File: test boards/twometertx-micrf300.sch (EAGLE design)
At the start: 12 parts

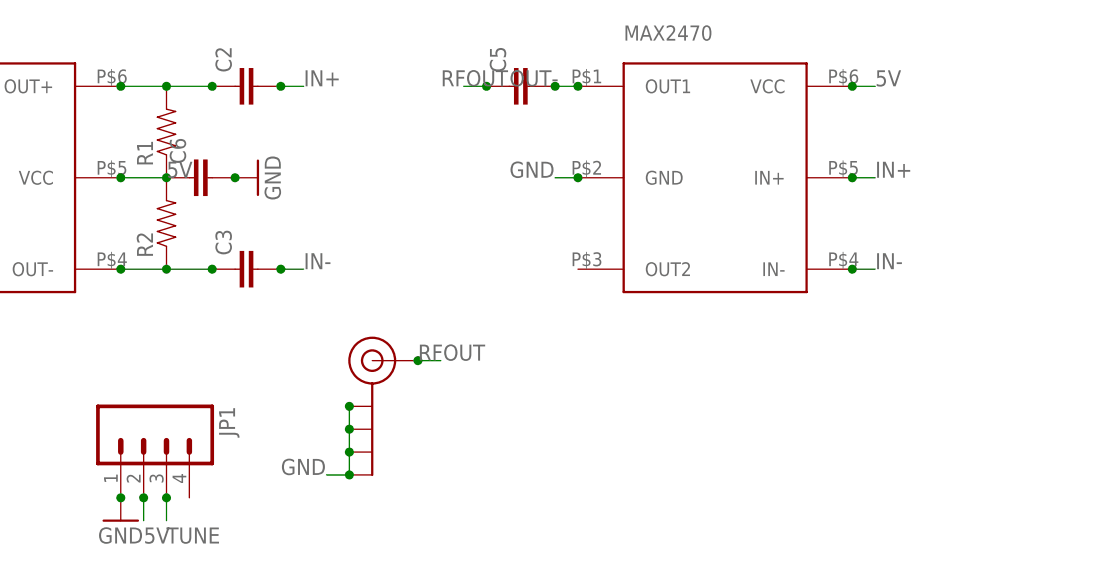
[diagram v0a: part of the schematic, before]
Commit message: updates
added twometertx-micrf300, changed layout of twometertx, changed led
layout on programmer shield to correct an error, added tracksoar v1.1
to swap power and ground pins on power input header
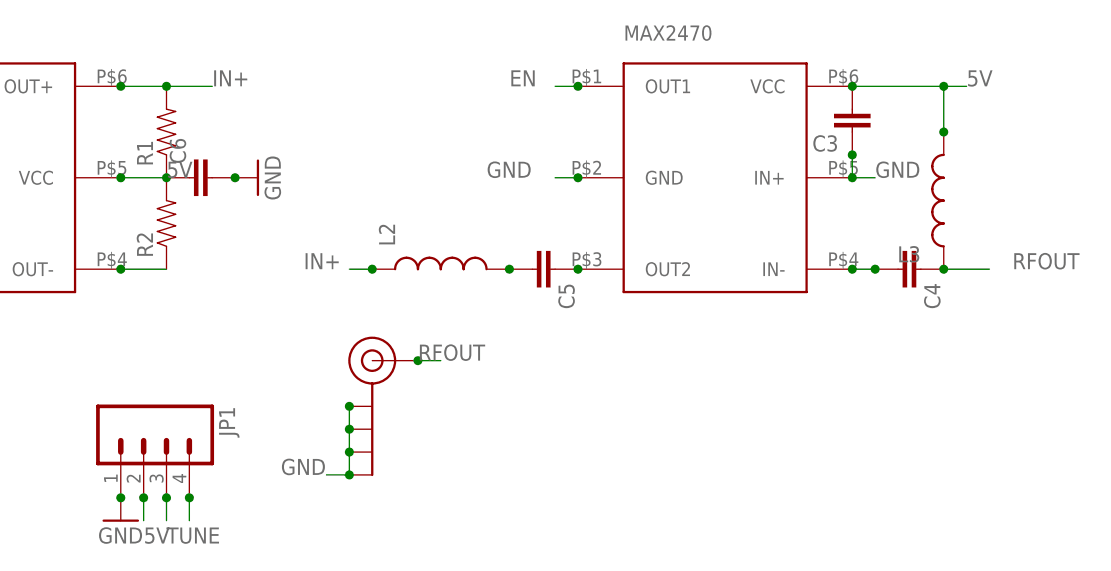
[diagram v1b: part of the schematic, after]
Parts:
- removed C2: (no value), SparkFun-Capacitors:CAP0805
- added C4: (no value), SparkFun-Capacitors:CAP0805
- added L2, L3: (no value), SparkFun-Passives:INDUCTOR0805
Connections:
- removed net IN-: C3.2, U$2.IN-
- removed net OUT-: C5.2, U$2.OUT1
- removed net THING: C2.1, R1.2, U$1.OUT+
- new net EN: JP1.4, U$2.OUT1
- new net N$1: C5.1, U$2.OUT2
- new net N$4: C5.2, L2.2
- net 5V: now also C3.2, L3.2
- net GND: now also C3.1, C4.2, U$2.IN+, U$2.IN-
- net IN+: now also L2.1, R1.2, U$1.OUT+; no longer C2.2, U$2.IN+
- net RFOUT: now also C4.1, L3.1; no longer C5.1
- net THING2: no longer C3.1
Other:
- moved on the sheet: C3, C5
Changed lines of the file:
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@@
 <part name="R1" library="SparkFun-Passives" deviceset="RESISTOR" device="0805-RES"/>
 <part name="R2" library="SparkFun-Passives" deviceset="RESISTOR" device="0805-RES"/>
-<part name="C2" library="SparkFun-Capacitors" deviceset="CAP" device="0805"/>
-<part name="C3" library="SparkFun-Capacitors" deviceset="CAP" device="0805"/>
 <part name="U$2" library="MAX2470" deviceset="MAX2470" device=""/>
-<part name="C5" library="SparkFun-Capacitors" deviceset="CAP" device="0805"/>
 <part name="J$1" library="SparkFun-Connectors" deviceset="SMA_EDGE" device=""/>
 <part name="JP1" library="SparkFun-Connectors" deviceset="M04" device="LONGPADS"/>
@@
 <part name="C6" library="SparkFun-Capacitors" deviceset="CAP" device="0805"/>
 <part name="GND3" library="SparkFun-Aesthetics" deviceset="GND" device=""/>
+<part name="L2" library="SparkFun-Passives" deviceset="INDUCTOR" device="0805"/>
+<part name="C3" library="SparkFun-Capacitors" deviceset="CAP" device="0805"/>
+<part name="C4" library="SparkFun-Capacitors" deviceset="CAP" device="0805"/>
+<part name="L3" library="SparkFun-Passives" deviceset="INDUCTOR" device="0805"/>
+<part name="C5" library="SparkFun-Capacitors" deviceset="CAP" device="0805"/>
 </parts>
 <sheets>
@@
 <instance part="R1" gate="G$1" x="63.5" y="55.88" rot="R90"/>
 <instance part="R2" gate="G$1" x="63.5" y="45.72" rot="R90"/>
-<instance part="C2" gate="G$1" x="73.66" y="60.96" rot="R90"/>
-<instance part="C3" gate="G$1" x="73.66" y="40.64" rot="R90"/>
 <instance part="U$2" gate="G$2" x="124.46" y="50.8" rot="R270"/>
-<instance part="C5" gate="G$1" x="104.14" y="60.96" rot="R90"/>
 <instance part="J$1" gate="1" x="86.36" y="30.48"/>
 <instance part="JP1" gate="G$1" x="60.96" y="20.32" rot="R270"/>
@@
 <instance part="C6" gate="G$1" x="68.58" y="50.8" rot="R90"/>
 <instance part="GND3" gate="1" x="73.66" y="50.8" rot="R90"/>
+<instance part="L2" gate="G$1" x="93.98" y="40.64" rot="R90"/>
+<instance part="C3" gate="G$1" x="139.7" y="58.42" rot="R180"/>
+<instance part="C4" gate="G$1" x="144.78" y="40.64" rot="R270"/>
+<instance part="L3" gate="G$1" x="149.86" y="48.26" rot="R180"/>
+<instance part="C5" gate="G$1" x="104.14" y="40.64" rot="R270"/>
 </instances>
 <busses>
@@
 <junction x="30.48" y="50.8"/>
 <junction x="10.16" y="48.26"/>
-</segment>
-<segment>
-<pinref part="U$2" gate="G$2" pin="GND"/>
-<wire x1="109.22" y1="50.8" x2="106.68" y2="50.8" width="0.1524" layer="91"/>
-<label x="101.6" y="50.8" size="1.778" layer="95"/>
-<junction x="109.22" y="50.8"/>
 </segment>
 <segment>
@@
 <junction x="71.12" y="50.8"/>
 </segment>
+<segment>
+<pinref part="U$2" gate="G$2" pin="GND"/>
+<wire x1="109.22" y1="50.8" x2="106.68" y2="50.8" width="0.1524" layer="91"/>
+<junction x="109.22" y="50.8"/>
+<label x="99.06" y="50.8" size="1.778" layer="95"/>
+</segment>
+<segment>
+<pinref part="U$2" gate="G$2" pin="IN-"/>
+<wire x1="139.7" y1="40.64" x2="142.24" y2="40.64" width="0.1524" layer="91"/>
+<junction x="139.7" y="40.64"/>
+<pinref part="C4" gate="G$1" pin="2"/>
+<junction x="142.24" y="40.64"/>
+</segment>
+<segment>
+<pinref part="U$2" gate="G$2" pin="IN+"/>
+<pinref part="C3" gate="G$1" pin="1"/>
+<wire x1="139.7" y1="50.8" x2="139.7" y2="53.34" width="0.1524" layer="91"/>
+<junction x="139.7" y="53.34"/>
+<wire x1="139.7" y1="50.8" x2="142.24" y2="50.8" width="0.1524" layer="91"/>
+<junction x="139.7" y="50.8"/>
+<label x="142.24" y="50.8" size="1.778" layer="95"/>
+</segment>
 </net>
 <net name="TUNE" class="0">
@@
 </segment>
 </net>
-<net name="THING" class="0">
-<segment>
-<pinref part="U$1" gate="G$1" pin="OUT+"/>
-<wire x1="58.42" y1="60.96" x2="63.5" y2="60.96" width="0.1524" layer="91"/>
-<junction x="58.42" y="60.96"/>
-<pinref part="R1" gate="G$1" pin="2"/>
-<junction x="63.5" y="60.96"/>
-<wire x1="63.5" y1="60.96" x2="68.58" y2="60.96" width="0.1524" layer="91"/>
-<pinref part="C2" gate="G$1" pin="1"/>
-<junction x="68.58" y="60.96"/>
-</segment>
-</net>
 <net name="THING2" class="0">
 <segment>
@@
 <junction x="58.42" y="40.64"/>
 <pinref part="R2" gate="G$1" pin="1"/>
-<junction x="63.5" y="40.64"/>
-<wire x1="63.5" y1="40.64" x2="68.58" y2="40.64" width="0.1524" layer="91"/>
-<pinref part="C3" gate="G$1" pin="1"/>
-<junction x="68.58" y="40.64"/>
 </segment>
 </net>
@@
 </segment>
 <segment>
-<pinref part="U$2" gate="G$2" pin="VCC"/>
-<wire x1="139.7" y1="60.96" x2="142.24" y2="60.96" width="0.1524" layer="91"/>
-<label x="142.24" y="60.96" size="1.778" layer="95"/>
-<junction x="139.7" y="60.96"/>
-</segment>
-<segment>
 <wire x1="60.96" y1="12.7" x2="60.96" y2="15.24" width="0.1524" layer="91"/>
 <label x="60.96" y="10.16" size="1.778" layer="95"/>
@@
 <junction x="60.96" y="15.24"/>
 </segment>
+<segment>
+<pinref part="U$2" gate="G$2" pin="VCC"/>
+<wire x1="139.7" y1="60.96" x2="149.86" y2="60.96" width="0.1524" layer="91"/>
+<junction x="139.7" y="60.96"/>
+<label x="152.4" y="60.96" size="1.778" layer="95"/>
+<pinref part="C3" gate="G$1" pin="2"/>
+<pinref part="L3" gate="G$1" pin="2"/>
+<wire x1="149.86" y1="55.88" x2="149.86" y2="60.96" width="0.1524" layer="91"/>
+<wire x1="149.86" y1="60.96" x2="152.4" y2="60.96" width="0.1524" layer="91"/>
+<junction x="149.86" y="55.88"/>
+<junction x="149.86" y="60.96"/>
+</segment>
 </net>
 <net name="IN+" class="0">
 <segment>
-<pinref part="C2" gate="G$1" pin="2"/>
-<wire x1="76.2" y1="60.96" x2="78.74" y2="60.96" width="0.1524" layer="91"/>
-<junction x="76.2" y="60.96"/>
-<label x="78.74" y="60.96" size="1.778" layer="95"/>
-</segment>
-<segment>
-<pinref part="U$2" gate="G$2" pin="IN+"/>
-<wire x1="139.7" y1="50.8" x2="142.24" y2="50.8" width="0.1524" layer="91"/>
-<label x="142.24" y="50.8" size="1.778" layer="95"/>
-<junction x="139.7" y="50.8"/>
-</segment>
-</net>
-<net name="IN-" class="0">
-<segment>
-<pinref part="C3" gate="G$1" pin="2"/>
-<wire x1="76.2" y1="40.64" x2="78.74" y2="40.64" width="0.1524" layer="91"/>
-<junction x="76.2" y="40.64"/>
+<pinref part="L2" gate="G$1" pin="1"/>
+<wire x1="86.36" y1="40.64" x2="83.82" y2="40.64" width="0.1524" layer="91"/>
+<junction x="86.36" y="40.64"/>
 <label x="78.74" y="40.64" size="1.778" layer="95"/>
 </segment>
 <segment>
-<pinref part="U$2" gate="G$2" pin="IN-"/>
-<wire x1="139.7" y1="40.64" x2="142.24" y2="40.64" width="0.1524" layer="91"/>
-<label x="142.24" y="40.64" size="1.778" layer="95"/>
-<junction x="139.7" y="40.64"/>
-</segment>
-</net>
-<net name="OUT-" class="0">
-<segment>
-<pinref part="U$2" gate="G$2" pin="OUT1"/>
-<wire x1="109.22" y1="60.96" x2="106.68" y2="60.96" width="0.1524" layer="91"/>
-<label x="101.6" y="60.96" size="1.778" layer="95"/>
-<pinref part="C5" gate="G$1" pin="2"/>
-<junction x="106.68" y="60.96"/>
-<junction x="109.22" y="60.96"/>
+<pinref part="U$1" gate="G$1" pin="OUT+"/>
+<wire x1="58.42" y1="60.96" x2="63.5" y2="60.96" width="0.1524" layer="91"/>
+<junction x="58.42" y="60.96"/>
+<pinref part="R1" gate="G$1" pin="2"/>
+<junction x="63.5" y="60.96"/>
+<wire x1="63.5" y1="60.96" x2="68.58" y2="60.96" width="0.1524" layer="91"/>
+<label x="68.58" y="60.96" size="1.778" layer="95"/>
 </segment>
 </net>
@@
 </segment>
 <segment>
+<pinref part="C4" gate="G$1" pin="1"/>
+<wire x1="149.86" y1="40.64" x2="154.94" y2="40.64" width="0.1524" layer="91"/>
+<pinref part="L3" gate="G$1" pin="1"/>
+<junction x="149.86" y="40.64"/>
+<label x="157.48" y="40.64" size="1.778" layer="95"/>
+</segment>
+</net>
+<net name="EN" class="0">
+<segment>
+<pinref part="JP1" gate="G$1" pin="4"/>
+<wire x1="66.04" y1="15.24" x2="66.04" y2="12.7" width="0.1524" layer="91"/>
+<junction x="66.04" y="15.24"/>
+</segment>
+<segment>
+<pinref part="U$2" gate="G$2" pin="OUT1"/>
+<wire x1="109.22" y1="60.96" x2="106.68" y2="60.96" width="0.1524" layer="91"/>
+<junction x="109.22" y="60.96"/>
+<label x="101.6" y="60.96" size="1.778" layer="95"/>
+</segment>
+</net>
+<net name="N$1" class="0">
+<segment>
+<pinref part="U$2" gate="G$2" pin="OUT2"/>
 <pinref part="C5" gate="G$1" pin="1"/>
-<wire x1="99.06" y1="60.96" x2="96.52" y2="60.96" width="0.1524" layer="91"/>
-<junction x="99.06" y="60.96"/>
-<label x="93.98" y="60.96" size="1.778" layer="95"/>
-</segment>
-</net>
+<junction x="109.22" y="40.64"/>
+</segment>
+</net>
+<net name="N$4" class="0">
+<segment>
+<pinref part="L2" gate="G$1" pin="2"/>
+<pinref part="C5" gate="G$1" pin="2"/>
+<junction x="101.6" y="40.64"/>
+</segment>
+</net>

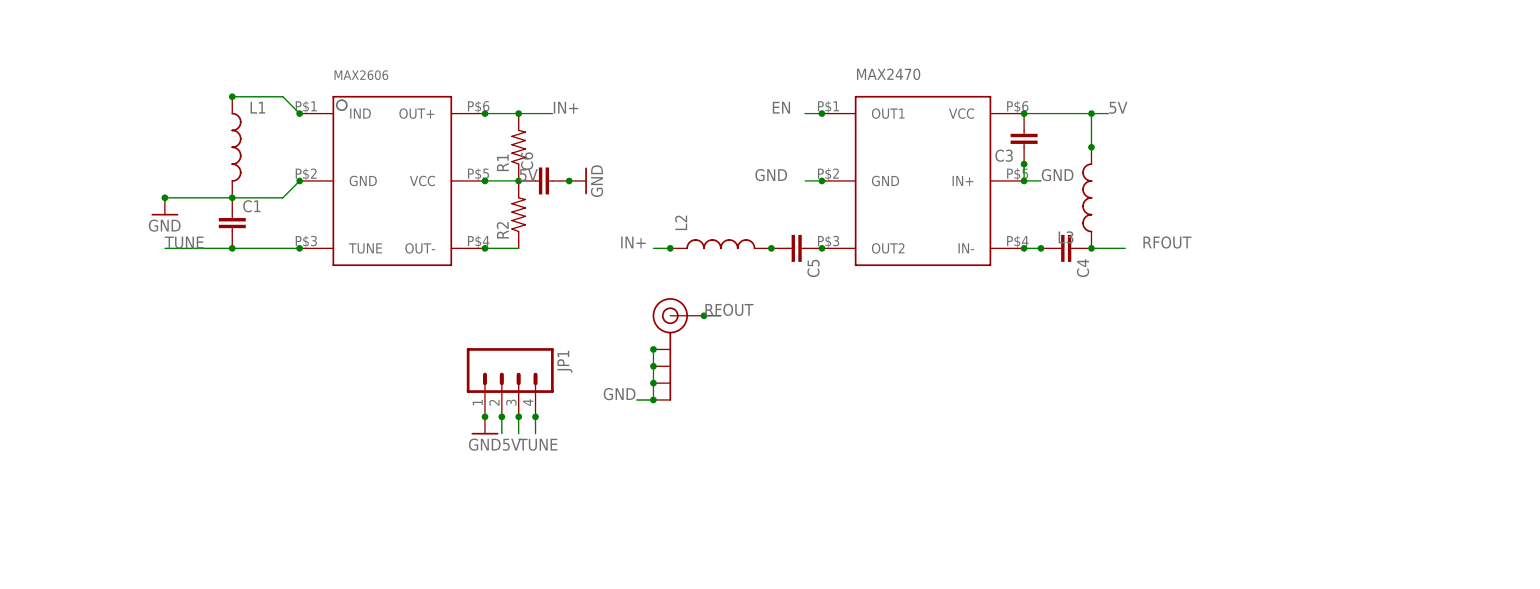
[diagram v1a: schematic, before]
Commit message: resolved 1.6.5+ compiling issues
resolved issues in afsk_avr.cpp / h that prevented the firmware from
compiling in 1.6.5+
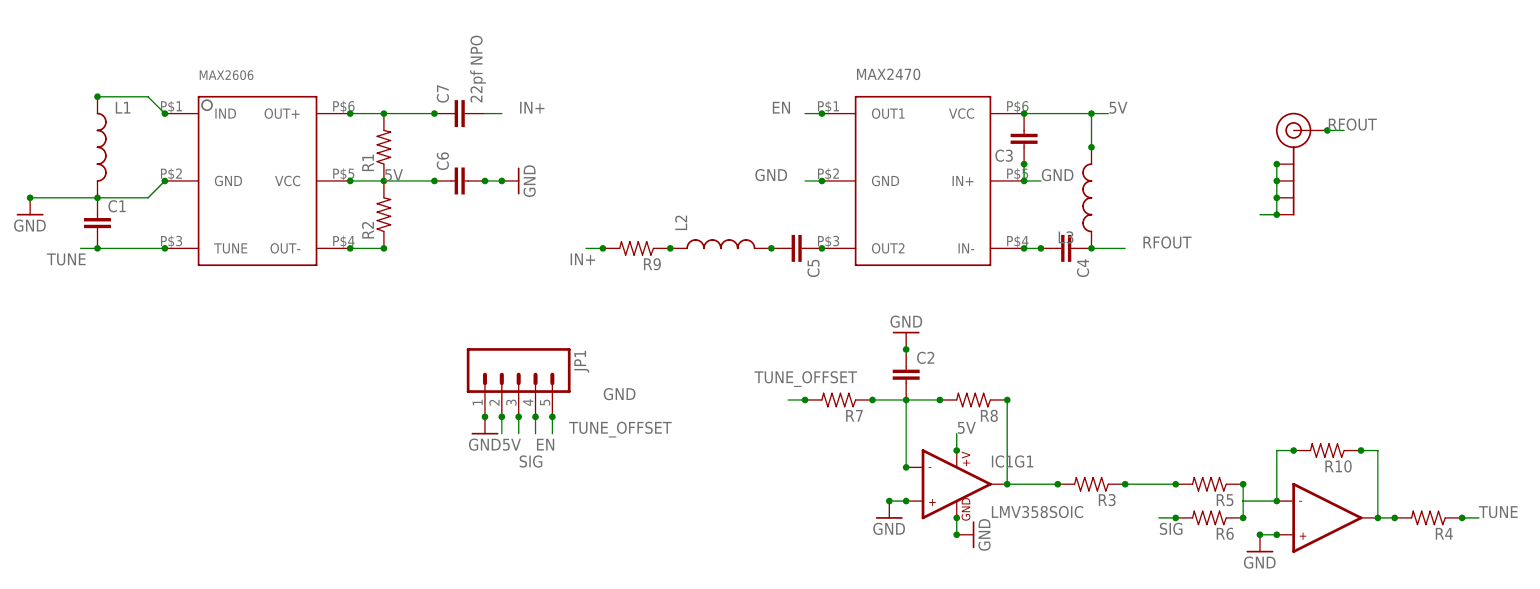
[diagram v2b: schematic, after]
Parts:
- added C2: (no value), SparkFun-Capacitors:CAP0805
- added C7: 22pf NPO, SparkFun-Capacitors:CAP0805
- added IC1: LMV358SOIC, SparkFun-AnalogIC:LMV358SOIC
- added R10, R3, R4, R5, R6, R7, R8, R9: (no value), SparkFun-Passives:RESISTOR0805-RES
- JP1: device SparkFun-Connectors:M04LONGPADS -> SparkFun-Connectors:M05PTH_LONGPADS
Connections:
- new net N$11: IC1G1.OUT1, R3.2, R8.1
- new net N$3: C2.2, IC1G1.-IN1, R7.1, R8.2
- new net N$5: R3.1, R5.2
- new net N$6: IC1G2.OUT2, R10.1, R4.2
- new net N$7: IC1G2.-IN2, R10.2, R5.1, R6.1
- new net N$8: L2.1, R9.1
- new net N$9: C7.1, R1.2, U$1.OUT+
- new net SIG: JP1.3, R6.2
- new net TUNE_OFFSET: JP1.5, R7.2
- net 5V: now also IC1G1.+V
- net GND: now also C2.1, IC1G1.+IN1, IC1G1.GND, IC1G2.+IN2
- net IN+: now also C7.2, R9.2; no longer L2.1, R1.2, U$1.OUT+
- net TUNE: now also R4.1; no longer JP1.3
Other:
- moved on the sheet: C1, C6, L1, R1, R2
